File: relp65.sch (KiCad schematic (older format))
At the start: 14 parts

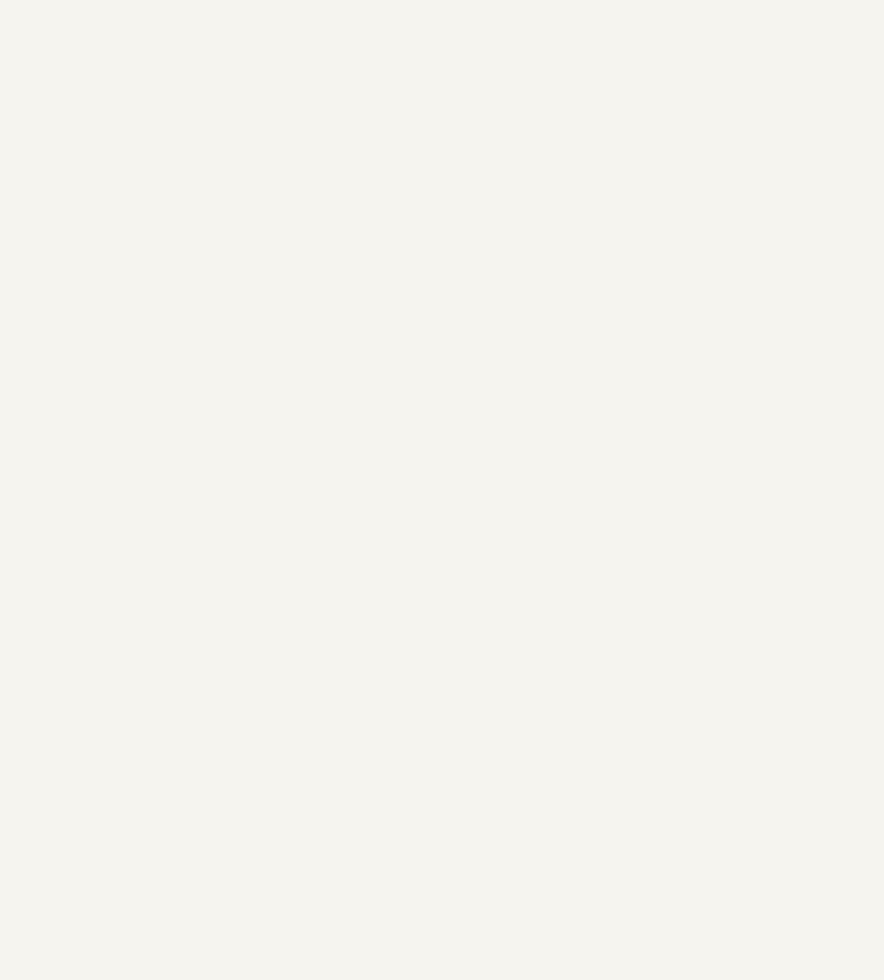
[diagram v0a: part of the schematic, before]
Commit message: ESD Protection
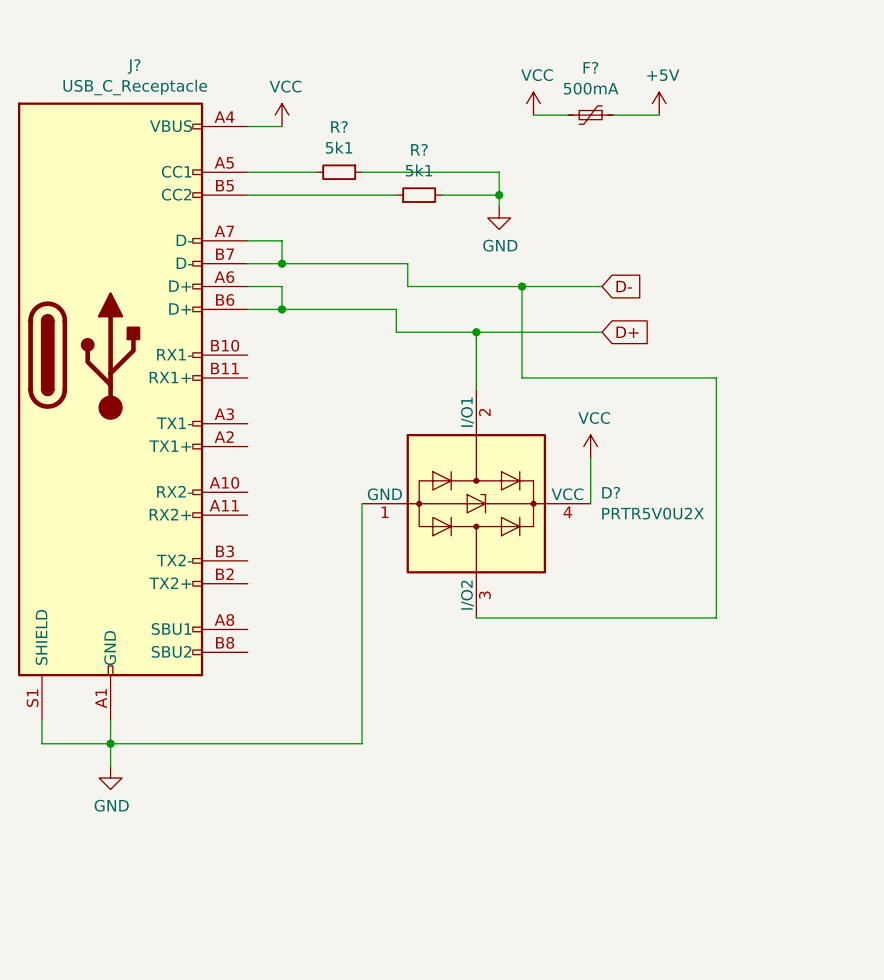
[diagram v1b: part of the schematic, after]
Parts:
- added D?: PRTR5V0U2X, Package_TO_SOT_SMD:SOT-143, symbol Power_Protection:PRTR5V0U2X
- added F?: 500mA, symbol Device:Polyfuse_Small
- added J?: USB_C_Receptacle, symbol Connector:USB_C_Receptacle
- added R? (x2): 5k1, symbol Device:R_Small
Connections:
- net +5V: now also F?.1
- net D+: now also D?.2 (I/O1), J?.A6 (D+), J?.B6 (D+)
- net D-: now also D?.3 (I/O2), J?.A7 (D-), J?.B7 (D-)
- net GND: now also D?.1 (GND), J?.A1 (GND), J?.A12 (GND), J?.B1 (GND), J?.B12 (GND), J?.S1 (SHIELD), R?.1, R?.2
- new net: J?.A5 (CC1), R?.2
- new net: J?.B5 (CC2), R?.1
- new net VCC: D?.4 (VCC), F?.2, J?.A4 (VBUS), J?.A9 (VBUS), J?.B4 (VBUS), J?.B9 (VBUS)
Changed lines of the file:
@@
 	0    -1   -1   0
 $EndComp
+$Comp
+L Connector:USB_C_Receptacle J?
+U 1 1 5E727671
+P 1550 1950
+F 0 "J?" H 1657 3217 50  0000 C CNN
+F 1 "USB_C_Receptacle" H 1657 3126 50  0000 C CNN
+F 2 "" H 1700 1950 50  0001 C CNN
+F 3 "https://www.usb.org/sites/default/files/documents/usb_type-c.zip" H 1700 1950 50  0001 C CNN
+	1    1550 1950
+	1    0    0    -1
+$EndComp
+$Comp
+L power:GND #PWR?
+U 1 1 5E72F7BF
+P 1550 3750
+F 0 "#PWR?" H 1550 3500 50  0001 C CNN
+F 1 "GND" H 1555 3577 50  0000 C CNN
+F 2 "" H 1550 3750 50  0001 C CNN
+F 3 "" H 1550 3750 50  0001 C CNN
+	1    1550 3750
+	1    0    0    -1
+$EndComp
+Wire Wire Line
+	1550 3750 1550 3650
+Wire Wire Line
+	1550 3650 1250 3650
+Wire Wire Line
+	1250 3650 1250 3550
+Connection ~ 1550 3650
+Wire Wire Line
+	1550 3650 1550 3550
+Wire Wire Line
+	2150 1650 2300 1650
+Wire Wire Line
+	2300 1650 2300 1750
+Wire Wire Line
+	2300 1750 2150 1750
+Wire Wire Line
+	2150 1450 2300 1450
+Wire Wire Line
+	2300 1450 2300 1550
+Wire Wire Line
+	2300 1550 2150 1550
+$Comp
+L Device:R_Small R?
+U 1 1 5E7C6785
+P 2550 1150
+F 0 "R?" V 2354 1150 50  0000 C CNN
+F 1 "5k1" V 2445 1150 50  0000 C CNN
+F 2 "" H 2550 1150 50  0001 C CNN
+F 3 "~" H 2550 1150 50  0001 C CNN
+	1    2550 1150
+	0    1    1    0
+$EndComp
+$Comp
+L Device:R_Small R?
+U 1 1 5E7C77A5
+P 2900 1250
+F 0 "R?" V 3096 1250 50  0000 C CNN
+F 1 "5k1" V 3005 1250 50  0000 C CNN
+F 2 "" H 2900 1250 50  0001 C CNN
+F 3 "~" H 2900 1250 50  0001 C CNN
+	1    2900 1250
+	0    -1   -1   0
+$EndComp
+$Comp
+L power:GND #PWR?
+U 1 1 5E7C9611
+P 3250 1300
+F 0 "#PWR?" H 3250 1050 50  0001 C CNN
+F 1 "GND" H 3255 1127 50  0000 C CNN
+F 2 "" H 3250 1300 50  0001 C CNN
+F 3 "" H 3250 1300 50  0001 C CNN
+	1    3250 1300
+	1    0    0    -1
+$EndComp
+Wire Wire Line
+	2150 1150 2450 1150
+Wire Wire Line
+	2650 1150 3250 1150
+Wire Wire Line
+	3250 1150 3250 1250
+Wire Wire Line
+	3000 1250 3250 1250
+Connection ~ 3250 1250
+Wire Wire Line
+	3250 1250 3250 1300
+Wire Wire Line
+	2800 1250 2150 1250
+$Comp
+L Power_Protection:PRTR5V0U2X D?
+U 1 1 5E7D05BA
+P 3150 2600
+F 0 "D?" V 3104 3144 50  0000 L CNN
+F 1 "PRTR5V0U2X" V 3195 3144 50  0000 L CNN
+F 2 "Package_TO_SOT_SMD:SOT-143" H 3210 2600 50  0001 C CNN
+F 3 "https://assets.nexperia.com/documents/data-sheet/PRTR5V0U2X.pdf" H 3210 2600 50  0001 C CNN
+	1    3150 2600
+	0    1    1    0
+$EndComp
+Wire Wire Line
+	1550 3650 2650 3650
+Wire Wire Line
+	2650 3650 2650 2600
+$Comp
+L power:VCC #PWR?
+U 1 1 5E7D6F6D
+P 2300 950
+F 0 "#PWR?" H 2300 800 50  0001 C CNN
+F 1 "VCC" H 2317 1123 50  0000 C CNN
+F 2 "" H 2300 950 50  0001 C CNN
+F 3 "" H 2300 950 50  0001 C CNN
+	1    2300 950
+	1    0    0    -1
+$EndComp
+Wire Wire Line
+	2150 950  2300 950
+$Comp
+L power:VCC #PWR?
+U 1 1 5E7D9E42
+P 3650 2400
+F 0 "#PWR?" H 3650 2250 50  0001 C CNN
+F 1 "VCC" H 3667 2573 50  0000 C CNN
+F 2 "" H 3650 2400 50  0001 C CNN
+F 3 "" H 3650 2400 50  0001 C CNN
+	1    3650 2400
+	1    0    0    -1
+$EndComp
+$Comp
+L power:VCC #PWR?
+U 1 1 5E7DC463
+P 3400 900
+F 0 "#PWR?" H 3400 750 50  0001 C CNN
+F 1 "VCC" H 3417 1073 50  0000 C CNN
+F 2 "" H 3400 900 50  0001 C CNN
+F 3 "" H 3400 900 50  0001 C CNN
+	1    3400 900
+	1    0    0    -1
+$EndComp
+$Comp
+L Device:Polyfuse_Small F?
+U 1 1 5E7DE1EC
+P 3650 900
+F 0 "F?" V 3445 900 50  0000 C CNN
+F 1 "500mA" V 3536 900 50  0000 C CNN
+F 2 "" H 3700 700 50  0001 L CNN
+F 3 "~" H 3650 900 50  0001 C CNN
+	1    3650 900
+	0    1    1    0
+$EndComp
+$Comp
+L power:+5V #PWR?
+U 1 1 5E7DF43F
+P 3950 900
+F 0 "#PWR?" H 3950 750 50  0001 C CNN
+F 1 "+5V" H 3965 1073 50  0000 C CNN
+F 2 "" H 3950 900 50  0001 C CNN
+F 3 "" H 3950 900 50  0001 C CNN
+	1    3950 900
+	1    0    0    -1
+$EndComp
+Wire Wire Line
+	3400 900  3550 900
+Wire Wire Line
+	3750 900  3950 900
+Wire Wire Line
+	3650 2400 3650 2600
+Wire Wire Line
+	2300 1550 2850 1550
+Wire Wire Line
+	2850 1550 2850 1650
+Wire Wire Line
+	2850 1650 3350 1650
+Connection ~ 2300 1550
+Wire Wire Line
+	2300 1750 2800 1750
+Wire Wire Line
+	2800 1750 2800 1850
+Wire Wire Line
+	2800 1850 3150 1850
+Connection ~ 2300 1750
+Text GLabel 3700 1650 2    50   Input ~ 0
+D-
+Text GLabel 3700 1850 2    50   Input ~ 0
+D+
+Wire Wire Line
+	3150 2100 3150 1850
+Connection ~ 3150 1850
+Wire Wire Line
+	3150 1850 3700 1850
+Wire Wire Line
+	3150 3100 4200 3100
+Wire Wire Line
+	4200 3100 4200 2050
+Wire Wire Line
+	4200 2050 3350 2050
+Wire Wire Line
+	3350 2050 3350 1650
+Connection ~ 3350 1650
+Wire Wire Line
+	3350 1650 3700 1650
 $EndSCHEMATC

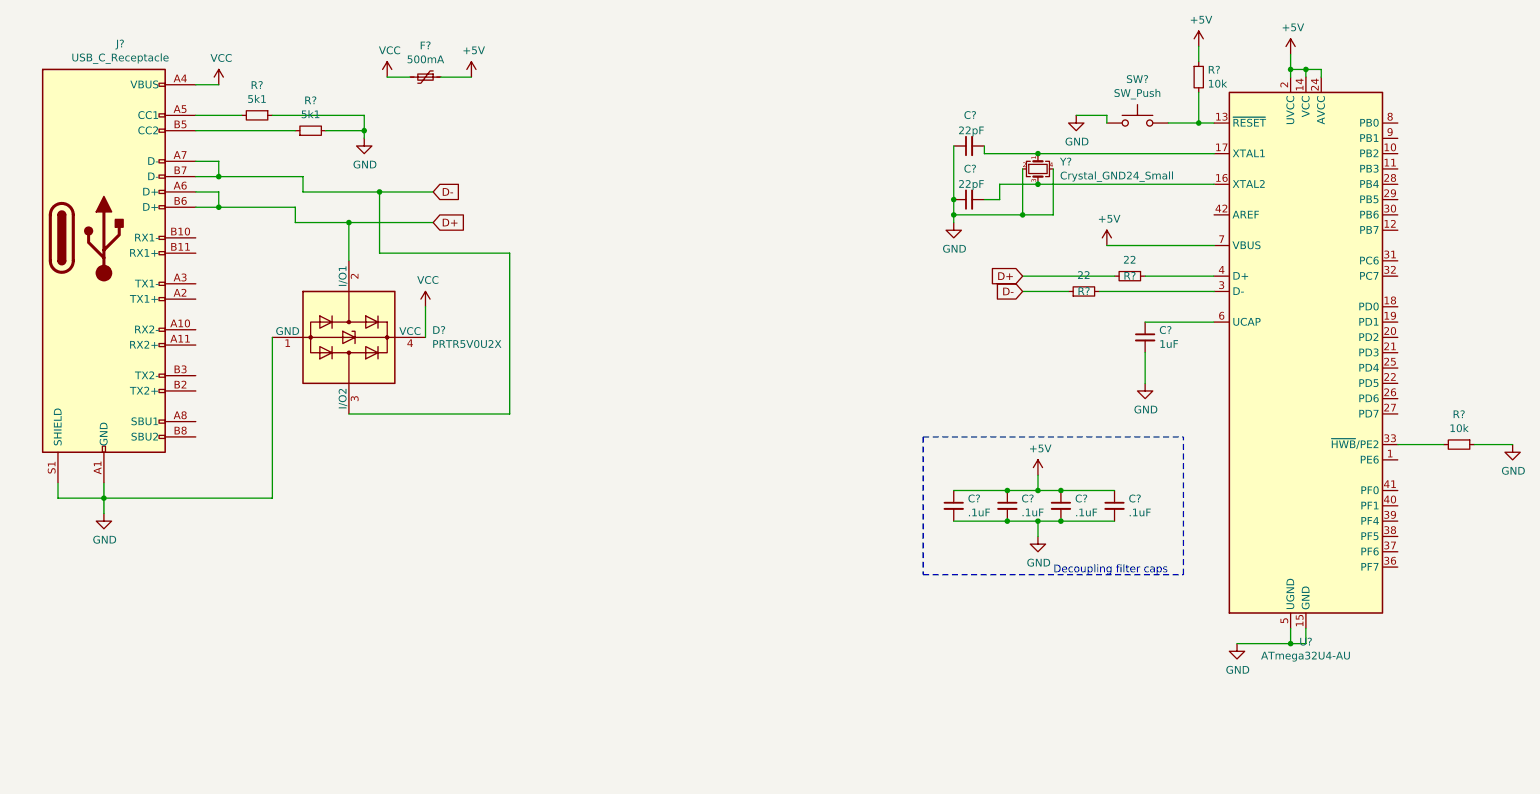
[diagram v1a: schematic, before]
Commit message: added keymatrix for Royal Alpha 600P
http://www.keyboard-layout-editor.com/#/gists/c176f41f556eae7376b5b4b1ef42a3b8
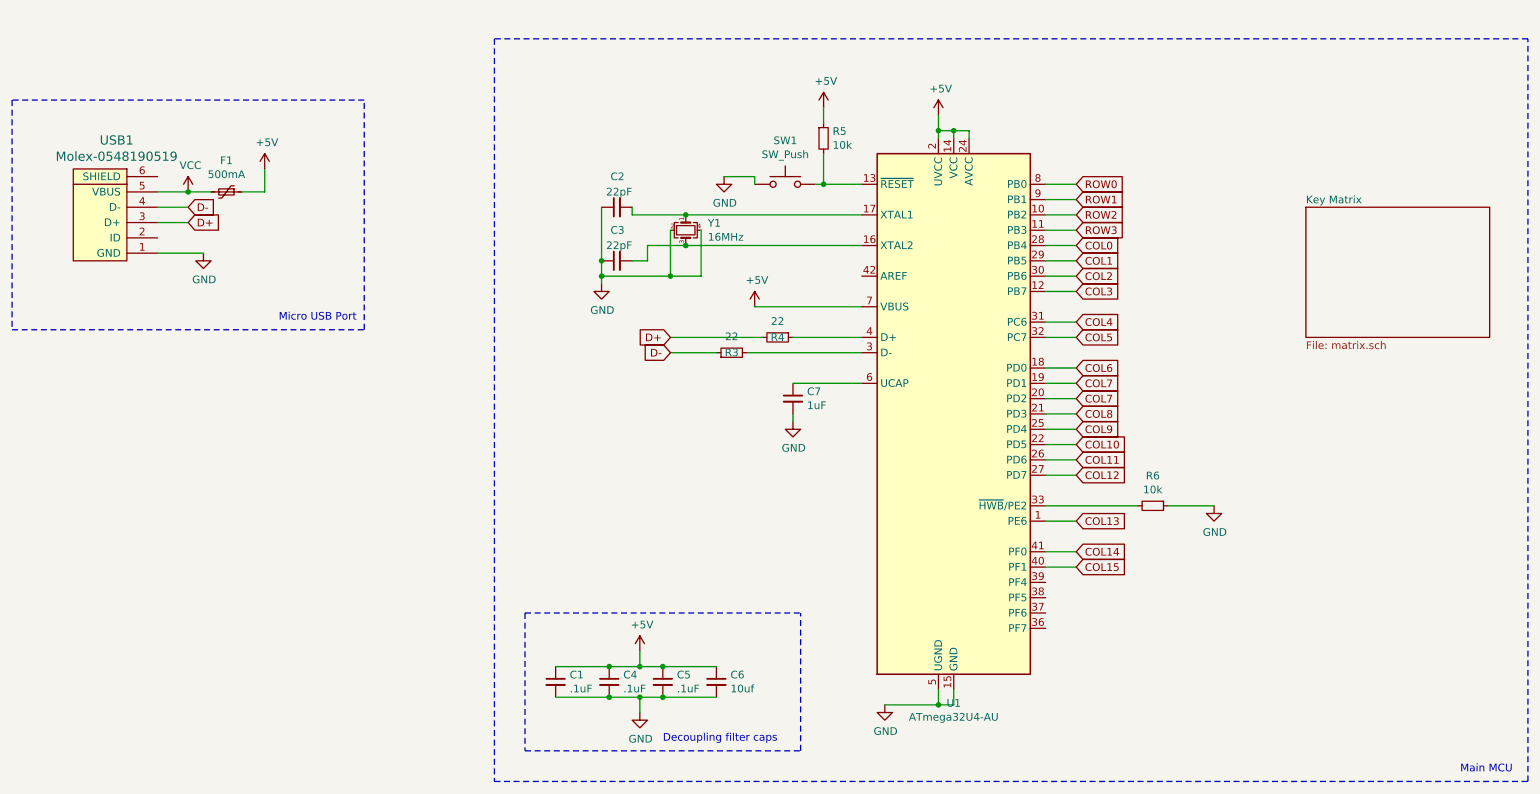
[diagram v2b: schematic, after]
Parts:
- removed D?: PRTR5V0U2X, Package_TO_SOT_SMD:SOT-143, symbol Power_Protection:PRTR5V0U2X
- removed F?: 500mA, symbol Device:Polyfuse_Small
- removed J?: USB_C_Receptacle, symbol Connector:USB_C_Receptacle
- removed R? (x2): 5k1, symbol Device:R_Small
- added F1: 500mA, Fuse:Fuse_1206_3216Metric, symbol Device:Polyfuse_Small
- added USB1: Molex-0548190519, random-keyboard-parts:Molex-0548190519, symbol random-keyboard-parts:Molex-0548190519
- C1, C2, C3, C4, C5, C7: renamed from C?; footprint (none) -> Capacitor_SMD:C_0805_2012Metric
- C6: renamed from C?; value .1uF -> 10uf; footprint (none) -> Capacitor_SMD:C_0805_2012Metric
- R3, R4, R5, R6: renamed from R?; footprint (none) -> Resistor_SMD:R_0805_2012Metric
- SW1: renamed from SW?; footprint (none) -> random-keyboard-parts:SKQG-1155865
- Y1: renamed from Y?; value Crystal_GND24_Small -> 16MHz; footprint (none) -> Crystal:Crystal_SMD_3225-4Pin_3.2x2.5mm
- gave numbers to parts that had none: 1
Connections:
- net +5V: now also F1.1
- net D+: now also USB1.3 (D+)
- net D-: now also USB1.4 (D-)
- net GND: now also USB1.1 (GND)
- net VCC: now also F1.2, USB1.5 (VBUS)
- net COL13: now reaches U1.1 (PE6)
- net ROW2: now reaches U1.10 (PB2)
- net ROW3: now reaches U1.11 (PB3)
- net COL3: now reaches U1.12 (PB7)
- net COL6: now reaches U1.18 (PD0)
- net COL7: now reaches U1.19 (PD1)
- net COL7: now also U1.20 (PD2)
- net COL8: now reaches U1.21 (PD3)
- net COL10: now reaches U1.22 (PD5)
- net COL9: now reaches U1.25 (PD4)
- net COL11: now reaches U1.26 (PD6)
- net COL12: now reaches U1.27 (PD7)
- net COL0: now reaches U1.28 (PB4)
- net COL1: now reaches U1.29 (PB5)
- net COL2: now reaches U1.30 (PB6)
- net COL4: now reaches U1.31 (PC6)
- net COL5: now reaches U1.32 (PC7)
- net COL15: now reaches U1.40 (PF1)
- net COL14: now reaches U1.41 (PF0)
- net ROW0: now reaches U1.8 (PB0)
- net ROW1: now reaches U1.9 (PB1)
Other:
- note added: "Main MCU"
- note added: "Micro USB Port"
- moved on the sheet: C1, C2, C3, C4, C5, C6, C7, R3, R4, R5, R6, SW1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
